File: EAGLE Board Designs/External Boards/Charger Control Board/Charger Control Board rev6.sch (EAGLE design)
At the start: 92 parts, among them U1 CPC1002N, U2 CDSOT23-T24CAN-Q

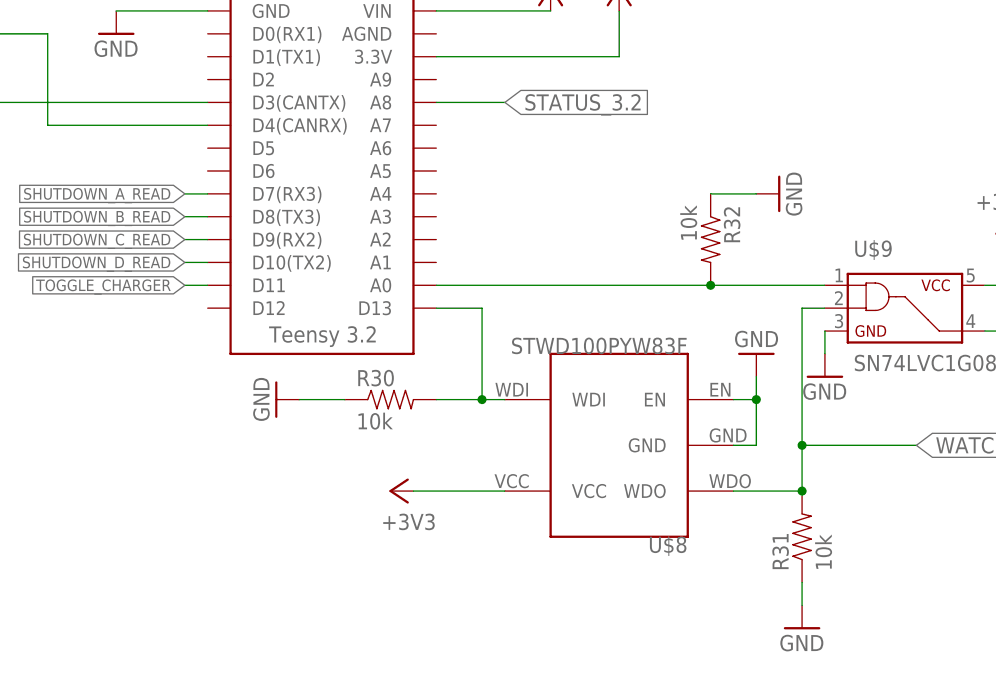
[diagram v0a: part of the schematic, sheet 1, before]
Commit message: redid teensy connections
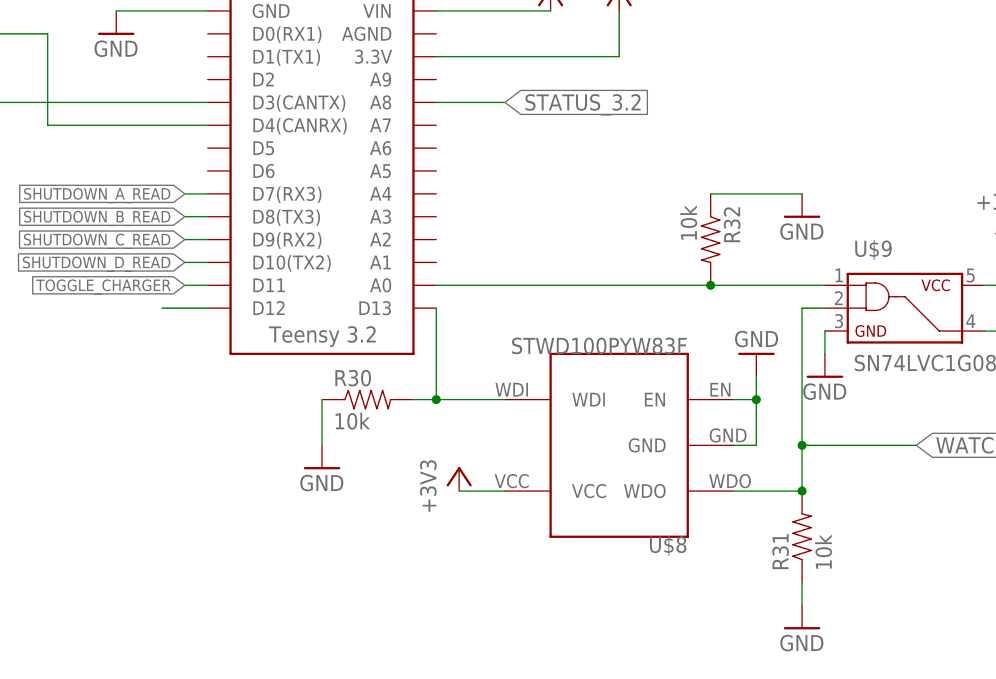
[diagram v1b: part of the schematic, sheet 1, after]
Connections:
- new net N$28: U$4.D12
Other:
- moved on the sheet: R30
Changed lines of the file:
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@@
 <attribute name="VALUE" x="168.275" y="33.655" size="1.778" layer="96"/>
 </instance>
-<instance part="R30" gate="G$1" x="116.84" y="30.48" smashed="yes">
-<attribute name="NAME" x="113.03" y="31.9786" size="1.778" layer="95"/>
-<attribute name="VALUE" x="113.03" y="27.178" size="1.778" layer="96"/>
-</instance>
-<instance part="GND29" gate="1" x="104.14" y="30.48" smashed="yes" rot="R270">
-<attribute name="VALUE" x="101.6" y="33.02" size="1.778" layer="96" rot="R270"/>
-</instance>
-<instance part="+3V1" gate="G$1" x="116.84" y="20.32" smashed="yes" rot="R90">
-<attribute name="VALUE" x="121.92" y="17.78" size="1.778" layer="96" rot="R180"/>
+<instance part="R30" gate="G$1" x="114.3" y="30.48" smashed="yes">
+<attribute name="NAME" x="110.49" y="31.9786" size="1.778" layer="95"/>
+<attribute name="VALUE" x="110.49" y="27.178" size="1.778" layer="96"/>
+</instance>
+<instance part="GND29" gate="1" x="109.22" y="22.86" smashed="yes">
+<attribute name="VALUE" x="106.68" y="20.32" size="1.778" layer="96"/>
+</instance>
+<instance part="+3V1" gate="G$1" x="124.46" y="22.86" smashed="yes">
+<attribute name="VALUE" x="121.92" y="17.78" size="1.778" layer="96" rot="R90"/>
 </instance>
 <instance part="R31" gate="G$1" x="162.56" y="15.24" smashed="yes" rot="R90">
@@
 <attribute name="VALUE" x="149.098" y="52.07" size="1.778" layer="96" rot="R270"/>
 </instance>
-<instance part="GND31" gate="1" x="160.02" y="53.34" smashed="yes" rot="R90">
-<attribute name="VALUE" x="162.56" y="50.8" size="1.778" layer="96" rot="R90"/>
+<instance part="GND31" gate="1" x="162.56" y="50.8" smashed="yes">
+<attribute name="VALUE" x="160.02" y="48.26" size="1.778" layer="96"/>
 </instance>
 <instance part="R33" gate="G$1" x="210.82" y="33.02" smashed="yes" rot="R90">
@@
 <pinref part="GND29" gate="1" pin="GND"/>
 <pinref part="R30" gate="G$1" pin="1"/>
-<wire x1="106.68" y1="30.48" x2="111.76" y2="30.48" width="0.1524" layer="91"/>
+<wire x1="109.22" y1="25.4" x2="109.22" y2="30.48" width="0.1524" layer="91"/>
 </segment>
 <segment>
@@
 <pinref part="GND31" gate="1" pin="GND"/>
 <pinref part="R32" gate="G$1" pin="1"/>
-<wire x1="157.48" y1="53.34" x2="152.4" y2="53.34" width="0.1524" layer="91"/>
+<wire x1="162.56" y1="53.34" x2="152.4" y2="53.34" width="0.1524" layer="91"/>
 </segment>
 <segment>
@@
 <pinref part="U$8" gate="G$1" pin="WDI"/>
 <pinref part="R30" gate="G$1" pin="2"/>
-<wire x1="121.92" y1="30.48" x2="127" y2="30.48" width="0.1524" layer="91"/>
+<wire x1="119.38" y1="30.48" x2="121.92" y2="30.48" width="0.1524" layer="91"/>
 <pinref part="U$4" gate="G$1" pin="D13"/>
-<wire x1="127" y1="30.48" x2="129.54" y2="30.48" width="0.1524" layer="91"/>
-<wire x1="121.92" y1="40.64" x2="127" y2="40.64" width="0.1524" layer="91"/>
-<wire x1="127" y1="40.64" x2="127" y2="30.48" width="0.1524" layer="91"/>
-<junction x="127" y="30.48"/>
+<wire x1="121.92" y1="30.48" x2="129.54" y2="30.48" width="0.1524" layer="91"/>
+<wire x1="121.92" y1="40.64" x2="121.92" y2="30.48" width="0.1524" layer="91"/>
+<junction x="121.92" y="30.48"/>
 </segment>
 </net>
@@
 <pinref part="+3V1" gate="G$1" pin="+3V3"/>
 <pinref part="U$8" gate="G$1" pin="VCC"/>
-<wire x1="119.38" y1="20.32" x2="129.54" y2="20.32" width="0.1524" layer="91"/>
+<wire x1="124.46" y1="20.32" x2="129.54" y2="20.32" width="0.1524" layer="91"/>
 </segment>
 <segment>
@@
 <net name="N$11" class="0">
 <segment>
-<pinref part="U$4" gate="G$1" pin="A0"/>
-<wire x1="121.92" y1="43.18" x2="152.4" y2="43.18" width="0.1524" layer="91"/>
 <pinref part="R32" gate="G$1" pin="2"/>
-<junction x="152.4" y="43.18"/>
 <pinref part="U$9" gate="G$1" pin="1"/>
 <wire x1="152.4" y1="43.18" x2="165.1" y2="43.18" width="0.1524" layer="91"/>
-</segment>
-</net>
+<junction x="152.4" y="43.18"/>
+<pinref part="U$4" gate="G$1" pin="A0"/>
+<wire x1="152.4" y1="43.18" x2="121.92" y2="43.18" width="0.1524" layer="91"/>
+</segment>
+</net>
+<net name="N$28" class="0">
+<segment>
+<pinref part="U$4" gate="G$1" pin="D12"/>
+<wire x1="91.44" y1="40.64" x2="96.52" y2="40.64" width="0.1524" layer="91"/>
+</segment>
+</net>

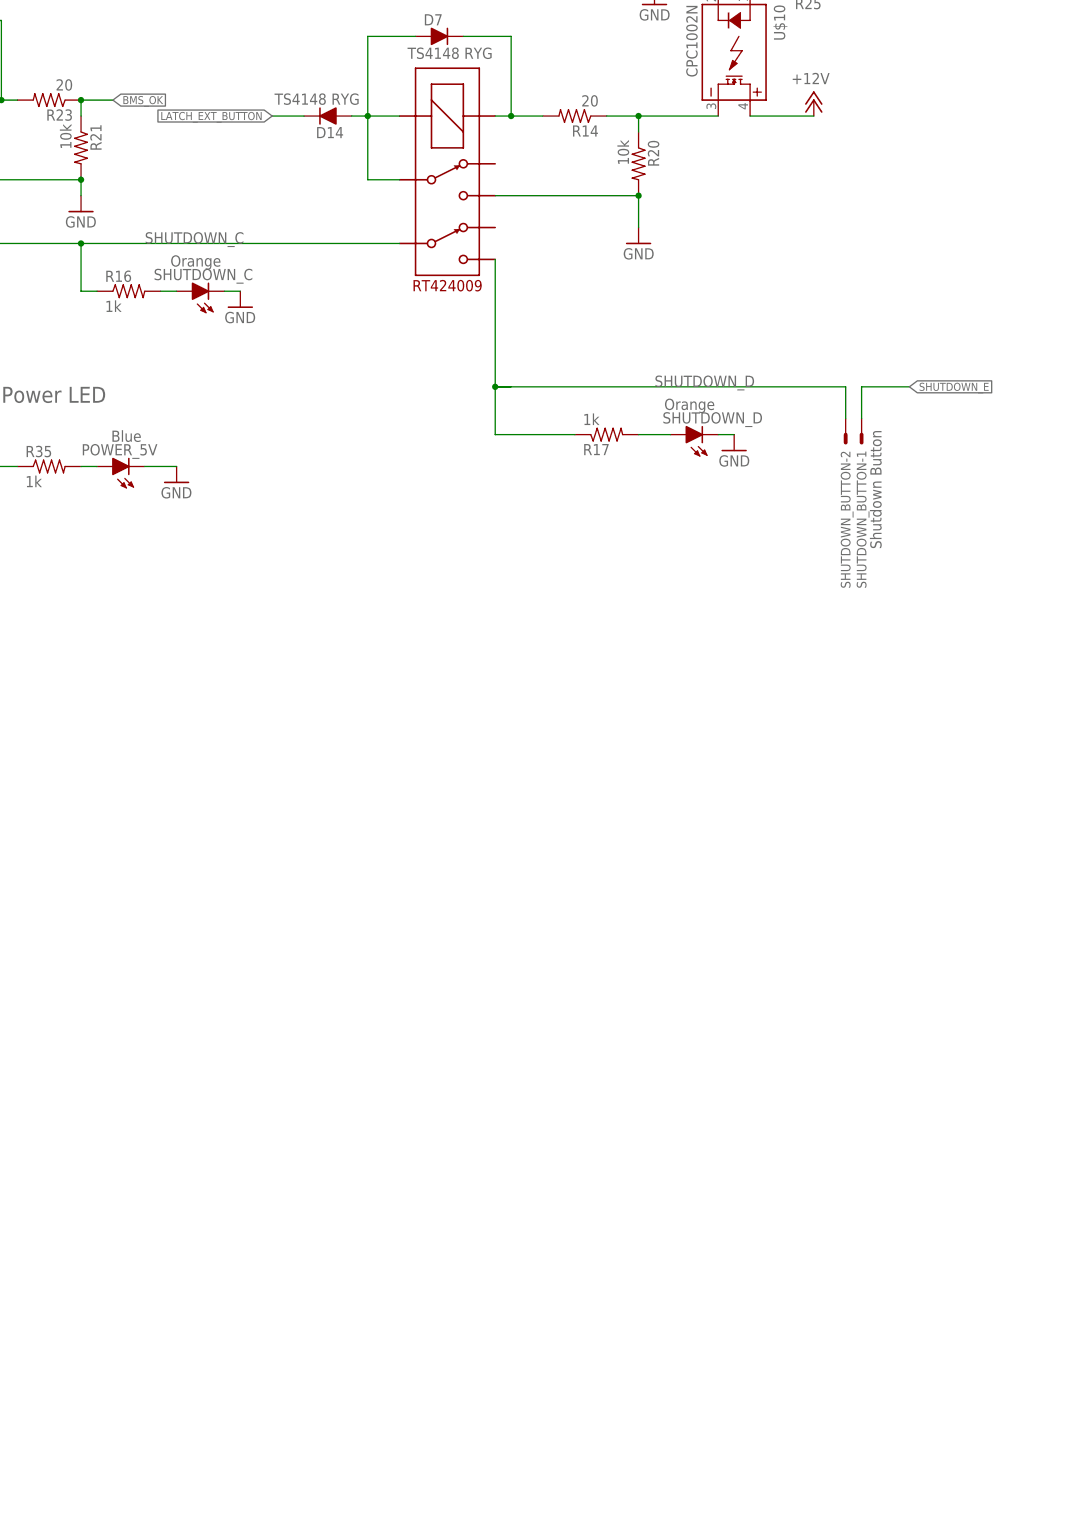
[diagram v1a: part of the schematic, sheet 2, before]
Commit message: made additional silkscreen changes and add 2 leds
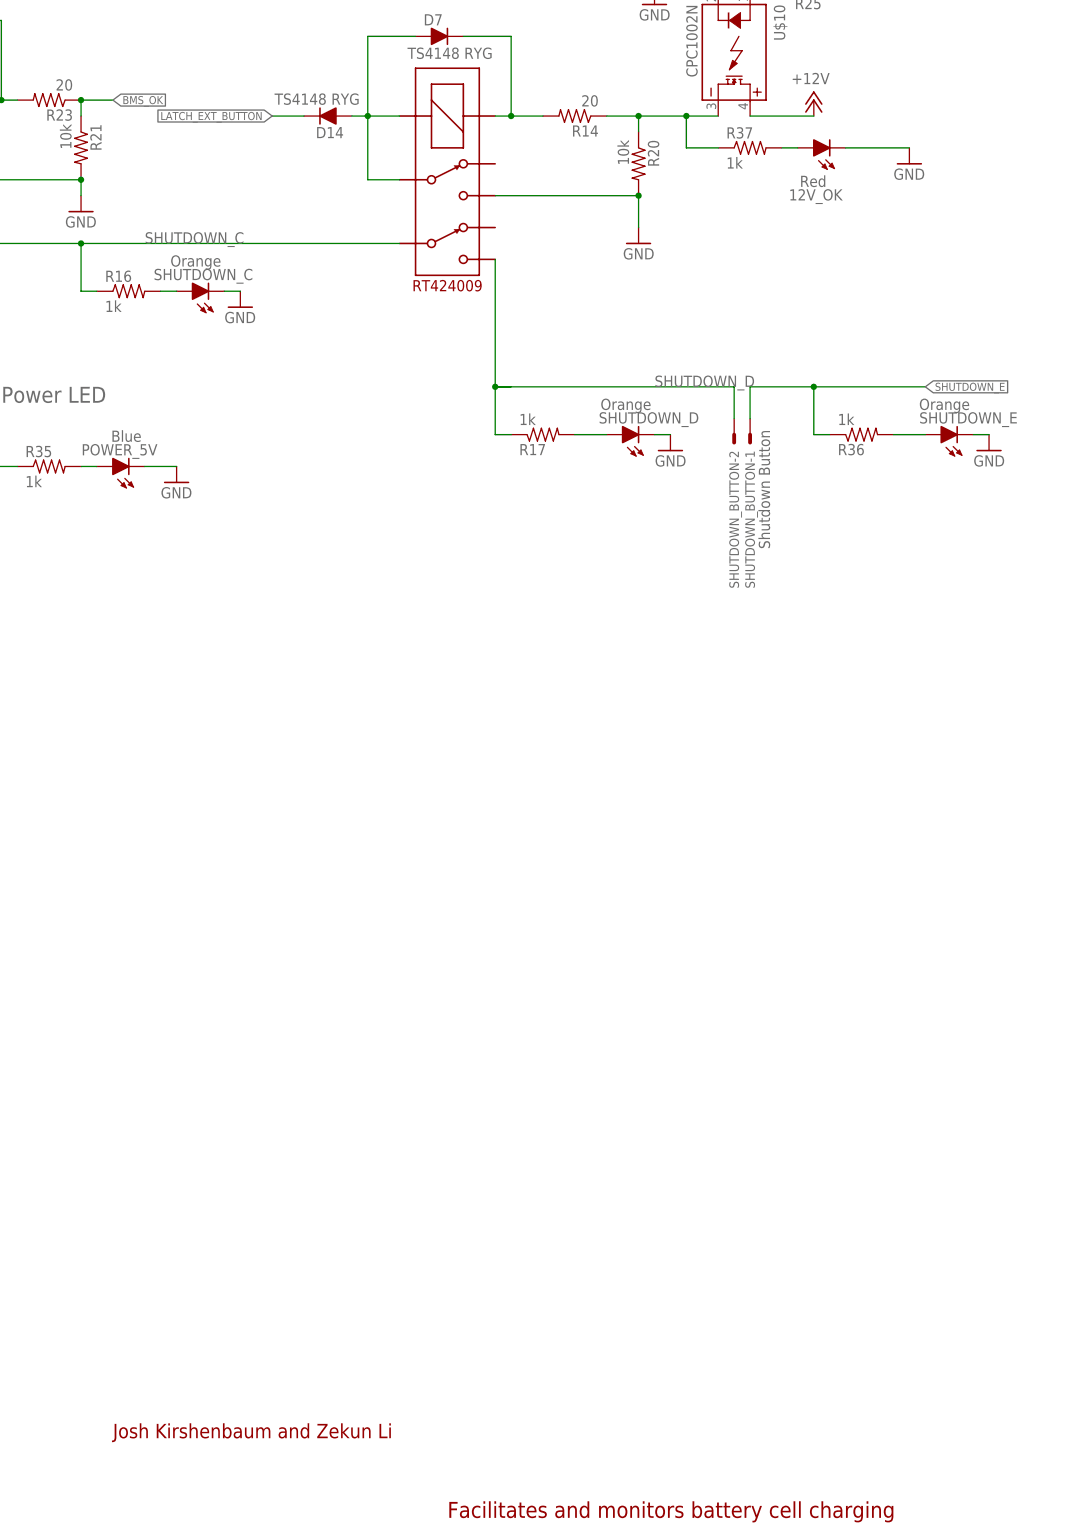
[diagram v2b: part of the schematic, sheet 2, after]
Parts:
- added 12V_OK: Red, HyTechDevices:LED-0805
- added R36, R37: 1k, HyTechDevices:RESISTOR0603-RES
- added SHUTDOWN_E: Orange, HyTechDevices:LED-0805
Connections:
- new net N$29: R36.2, SHUTDOWN_E.A
- new net N$34: 12V_OK.A, R37.2
- net GND: now also 12V_OK.C, SHUTDOWN_E.C
- net N$13: now also R37.1
- net SHUTDOWN_E: now also R36.1
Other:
- note added: "Facilitates and monitors battery cell charging"
- note added: "Josh Kirshenbaum and Zekun Li"
- moved on the sheet: R17, SHUTDOWN_BUTTON-1, SHUTDOWN_BUTTON-2, SHUTDOWN_D

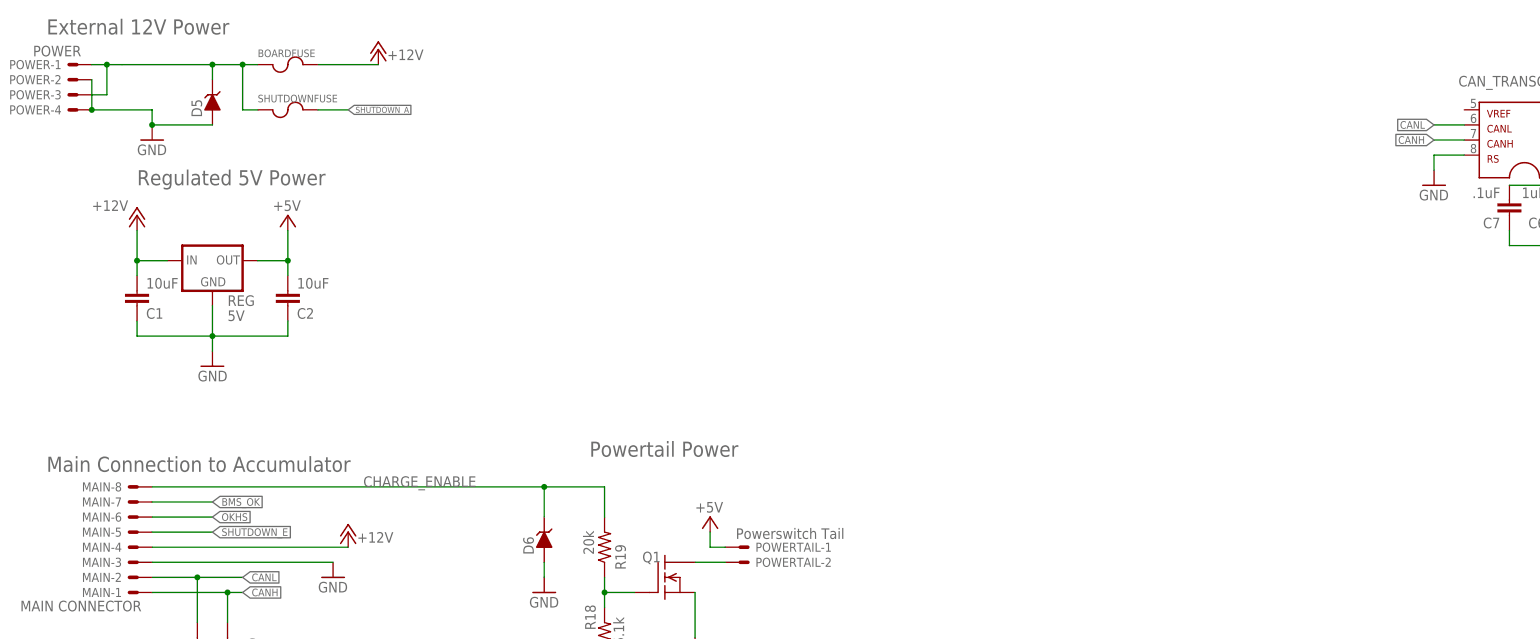
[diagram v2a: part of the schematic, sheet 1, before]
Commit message: Started to implement the e-fuse into the charger controller circuit
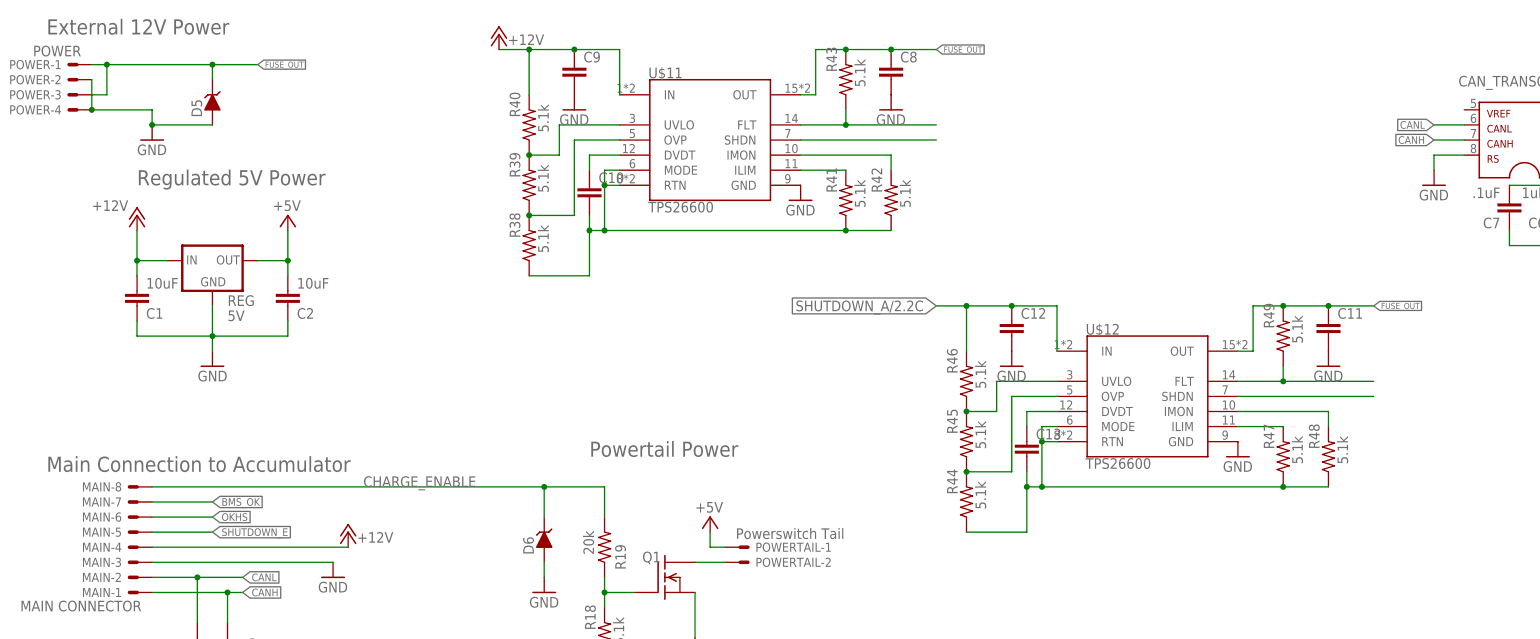
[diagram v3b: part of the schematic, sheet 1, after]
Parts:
- removed BOARDFUSE, SHUTDOWNFUSE: (no value), HyTechDevices:FUSE_MINIBLADE
- added C10, C11, C12, C13, C8, C9: (no value), HyTechDevices:CAP0805
- added R38, R39, R40, R41, R42, R43, R44, R45, R46, R47, R48, R49: 5.1k, HyTechDevices:RESISTOR0603-RES
- added U$11, U$12: TPS26600, HyTechDevices:TPS26600
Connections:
- removed net +12VIN: BOARDFUSE.1, D5.C, POWER-1.S, POWER-3.S, SHUTDOWNFUSE.1
- new net FUSE_OUT: C11.1, C8.1, D5.C, POWER-1.S, POWER-3.S, R43.2, R49.2, U$11.OUT, U$12.OUT
- new net N$35: C10.2, R38.1, R41.1, R42.1, U$11.MODE, U$11.RTN
- new net N$36: R38.2, R39.1, U$11.OVP
- new net N$37: R39.2, R40.1, U$11.UVLO
- new net N$38: R41.2, U$11.ILIM
- new net N$39: C13.2, R44.1, R47.1, R48.1, U$12.MODE, U$12.RTN
- new net N$40: R42.2, U$11.IMON
- new net N$41: R44.2, R45.1, U$12.OVP
- new net N$42: R43.1, U$11.FLT
- new net N$43: U$11.SHDN
- new net N$44: C10.1, U$11.DVDT
- new net N$45: R45.2, R46.1, U$12.UVLO
- new net N$46: R47.2, U$12.ILIM
- new net N$47: R48.2, U$12.IMON
- new net N$48: U$12.SHDN
- new net N$49: R49.1, U$12.FLT
- new net N$50: C13.1, U$12.DVDT
- new net SHUTDOWN_A/2.2C: C12.1, R46.2, U$12.IN
- net +12V: now also C9.1, R40.2, U$11.IN; no longer BOARDFUSE.2
- net GND: now also C11.2, C12.2, C8.2, C9.2, U$11.GND, U$12.GND
- net SHUTDOWN_A: no longer SHUTDOWNFUSE.2
